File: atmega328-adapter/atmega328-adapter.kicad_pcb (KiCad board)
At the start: 2 copper layers, 21.3 x 36.6 mm, 3 parts, among them U4 ATmega168A-A

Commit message: updated adapter
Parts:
- removed REF** (x2): PinHeader_1x14_P2.54mm_Vertical, Connector_PinHeader_2.54mm:PinHeader_1x14_P2.54mm_Vertical
- removed U4: ATmega168A-A, Package_QFP:TQFP-32_7x7mm_P0.8mm
- added J1: Conn_01x14, Connector_PinHeader_2.54mm:PinHeader_1x14_P2.54mm_Vertical, F.Cu at (114.9, 50.4)
- added J2: Conn_01x14, Connector_PinHeader_2.54mm:PinHeader_1x14_P2.54mm_Vertical, F.Cu at (122.5, 50.4)
- added U1: ATmega168A-A, Package_QFP:TQFP-32_7x7mm_P0.8mm, F.Cu at (129.7, 67.0)
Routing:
- net (no net): track 373.3 -> 0.00 mm, vias 28 -> 0
- net +5V: track 0.00 -> 38.6 mm
- net GND: track 0.00 -> 26.0 mm, vias 0 -> 1
- net /RESET: track 0.00 -> 22.3 mm
- net /PB0: track 0.00 -> 22.2 mm
- net /PD0: track 0.00 -> 19.4 mm
- net /PD7: track 0.00 -> 19.4 mm
- net /PC5: track 0.00 -> 17.2 mm
- net /PD1: track 0.00 -> 16.6 mm
- net /PD6: track 0.00 -> 16.5 mm
- net /PB1: track 0.00 -> 15.4 mm
- net /CS: track 0.00 -> 14.2 mm, vias 0 -> 1
- net /PC4: track 0.00 -> 14.2 mm, vias 0 -> 1
- net /PD2: track 0.00 -> 14.1 mm
- net /PD5: track 0.00 -> 13.9 mm
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- removed copper zone on B.Cu, net (none)
- removed copper zone on F.Cu, net (none)
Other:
- board size 21.3 x 36.6 mm -> 21.9 x 36.6 mm

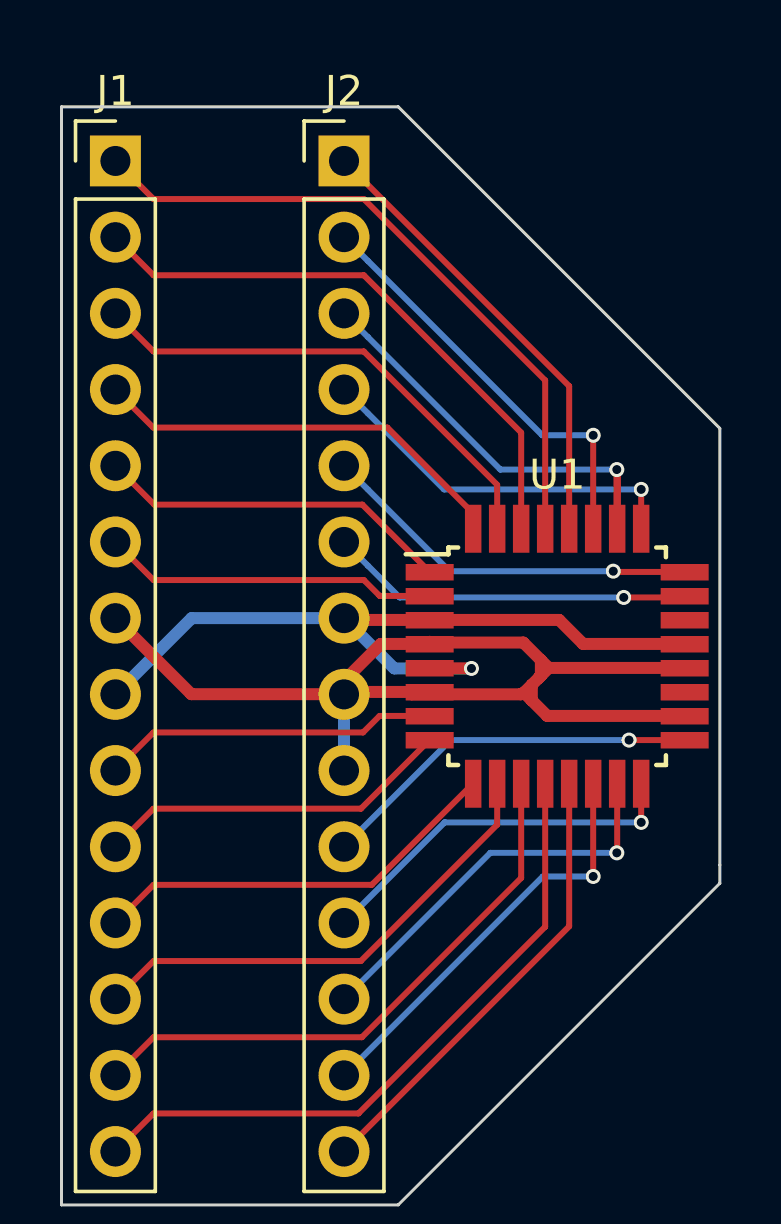
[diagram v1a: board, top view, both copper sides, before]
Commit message: silkscreen done
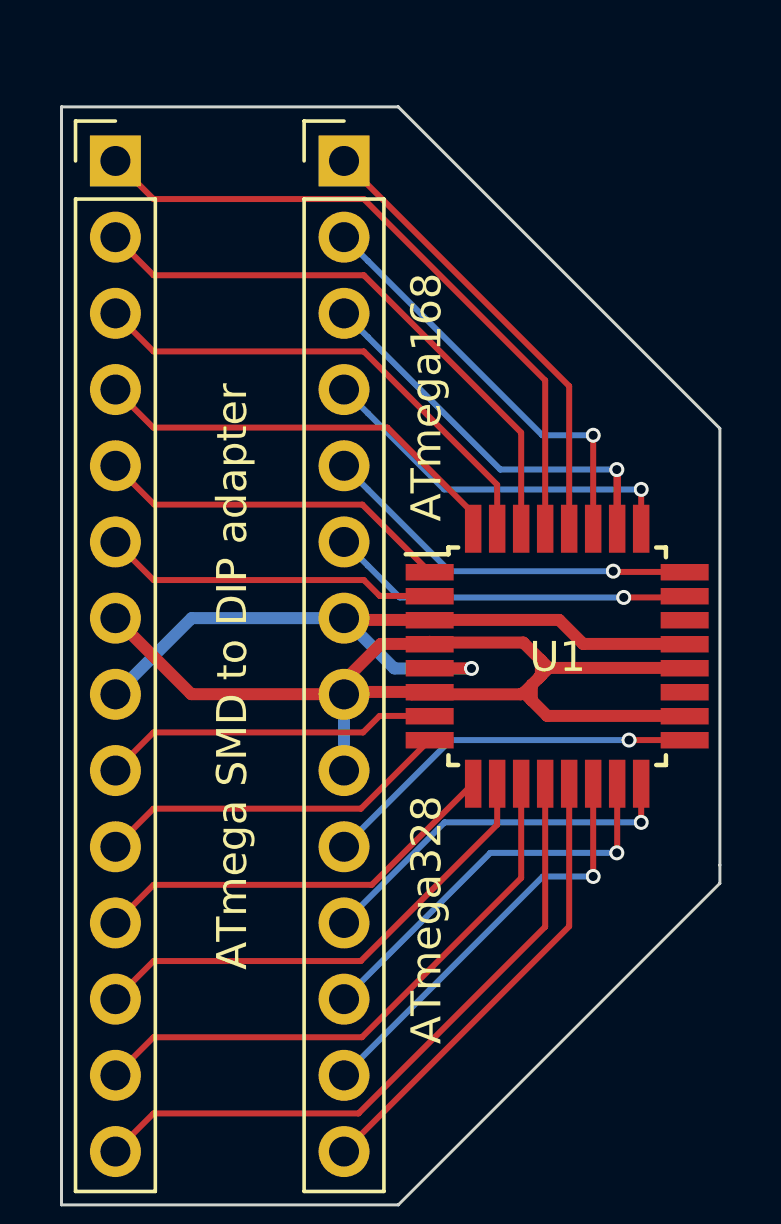
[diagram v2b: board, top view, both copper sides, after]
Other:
- board text added: "ATmega SMD to DIP adapter"
- board text added: "ATmega168"
- board text added: "ATmega328"
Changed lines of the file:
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@@
     (property "ki_keywords" "AVR 8bit Microcontroller MegaAVR")
     (attr smd)
-    (fp_text reference "U1" (at 0 -6.05) (layer "F.SilkS")
+    (fp_text reference "U1" (at 0.0126 0.0254) (layer "F.SilkS")
         (effects (font (size 1 1) (thickness 0.15)))
     )
@@
     (property "ki_keywords" "connector")
     (attr through_hole)
-    (fp_text reference "J1" (at 0 -2.33) (layer "F.SilkS")
+    (fp_text reference "J1" (at 0 -2.33) (layer "F.SilkS") hide
         (effects (font (size 1 1) (thickness 0.15)))
     )
@@
     (property "ki_keywords" "connector")
     (attr through_hole)
-    (fp_text reference "J2" (at 0 -2.33) (layer "F.SilkS")
+    (fp_text reference "J2" (at 0 -2.33) (layer "F.SilkS") hide
         (effects (font (size 1 1) (thickness 0.15)))
     )
@@
   (gr_line (start 135.0772 59.3598) (end 135.0772 73.914)
     (stroke (width 0.1) (type default)) (layer "Edge.Cuts"))
+  (gr_text "ATmega328" (at 125.8824 79.883 90) (layer "F.SilkS" knockout)
+    (effects (font (size 1 1) (thickness 0.15)) (justify left bottom))
+  )
+  (gr_text "ATmega168" (at 125.8824 58.3184 90) (layer "F.SilkS" knockout)
+    (effects (font (size 1 1) (thickness 0.15)) (justify bottom))
+  )
+  (gr_text "ATmega SMD to DIP adapter" (at 119.4054 77.408568 90) (layer "F.SilkS" knockout)
+    (effects (font (size 1 1) (thickness 0.15)) (justify left bottom))
+  )
   (segment (start 114.9277 60.6057) (end 114.9262 60.607) (width 0.25) (layer "F.Cu") (net 1))
   (segment (start 116.2244 61.8998) (end 114.929 60.6044) (width 0.2) (layer "F.Cu") (net 1))

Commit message: done
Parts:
- added G***: LOGO, LOGO, B.Cu at (129.7, 67.0)
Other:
- board text added: "Designed by:"

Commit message: kikit tabs
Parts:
- added REF**: Tab, kikit:Tab, F.Cu at (113.1, 57.3)
- added REF**: Tab, kikit:Tab, F.Cu at (125.5, 79.7)
- added REF**: Tab, kikit:Tab, F.Cu at (143.7, 63.1)
- added REF**: Tab, kikit:Tab, F.Cu at (137.3, 57.2)
- added REF**: Tab, kikit:Tab, F.Cu at (106.6, 63.1)
- moved J1 28.2 mm to (141.7, 59.3), turned to -90 degrees
- moved J2 25.3 mm to (141.7, 66.9), turned to -90 degrees
- moved G*** 8.37 mm to (125.2, 74.0), turned to 180 degrees
- moved U1 8.37 mm to (125.2, 74.0), turned to -90 degrees
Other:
- board size 21.9 x 36.6 mm -> 36.6 x 21.9 mm
